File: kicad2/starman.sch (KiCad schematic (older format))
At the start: 60 parts

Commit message: Placements of components and things
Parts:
- added C1, C2, C3, C4, C5, C6: C, Capacitor_SMD:C_0805_2012Metric, symbol Device:C
- added D61, D62, D63, D64, D65, D66, D67, D68, D69, D70, D71, D72, D73, D74, D75, D76, D77, D78, D79, D80, D81, D82, D83, D84, D85, D86, D87, D88, D89: LED, LED_SMD:LED_Osram_Lx_P47F_D2mm_ReverseMount, symbol Device:LED
- added J1: Barrel_Jack, Connector_BarrelJack:BarrelJack_CUI_PJ-036AH-SMT_Horizontal, symbol Connector:Barrel_Jack
- added P1: USB_C_Plug_USB2.0, Connector_USB:USB_C_Plug_JAE_DX07P024AJ1, symbol Connector:USB_C_Plug_USB2.0
- added U1: ESP32-S2-MINI-1, Espressif:ESP32-S2-MINI-1, symbol Espressif:ESP32-S2-MINI-1
- added U2, U3, U4, U5: TLC5947DAP, Package_SO:HTSSOP-32-1EP_6.1x11mm_P0.65mm_EP5.2x11mm_Mask4.11x4.36mm, symbol Driver_LED:TLC5947DAP
- added U6: LF33_TO220, Package_TO_SOT_SMD:SOT-223, symbol Regulator_Linear:LF33_TO220
- added U7: LF50_TO220, Package_TO_SOT_SMD:SOT-223, symbol Regulator_Linear:LF50_TO220
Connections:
- net labels added: +3.3V, +5V, BLANK, BOOT, GND, IREF, RESET, SCLK, SIN, USBDM, USBDP, XLAT
- wire segments 0 -> 296
- no-connect marks 0 -> 12

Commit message: Switch to PCA9959 as LED PWM driver
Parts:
- removed U2, U3, U4, U5: TLC5947DAP, Package_SO:HTSSOP-32-1EP_6.1x11mm_P0.65mm_EP5.2x11mm_Mask4.11x4.36mm, symbol Driver_LED:TLC5947DAP
- added C1: 10uF, Capacitor_SMD:C_0805_2012Metric, symbol Device:C
- added D100, D101, D102, D103, D104, D105, D106, D107, D108, D109, D110, D111, D112, D113, D114, D115, D116, D117, D118, D119, D120, D121, D122, D123, D124, D125, D126, D127, D128, D129, D130, D131, D132, D133, D134, D135, D136, D137, D138, D90, D91, D92, D93, D94, D95, D96, D97, D98, D99: LED, LED_SMD:LED_Osram_Lx_P47F_D2mm_ReverseMount, symbol Device:LED
- added R1, R2, R3: 5.1k, symbol Device:R
- added U2, U3, U4, U5, U8, U9: PCA9959, starman:QFN-40_EP_5x5_Pitch0.4mm, symbol starman:PCA9959
- C2: renamed from C1; value C -> 10uF
- C3: renamed from C2; value C -> 1uF
- P1: footprint Connector_USB:USB_C_Plug_JAE_DX07P024AJ1 -> Connector_USB:USB_C_Plug_Molex_105444; symbol Connector:USB_C_Plug_USB2.0 -> Connector:USB_C_Receptacle_USB2.0
- renumbered C3 to C4, C4 to C5, C5 to C6, C6 to C7
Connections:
- wire segments 296 -> 334
- no-connect marks 12 -> 7
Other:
- moved on the sheet: C2, C3, D1, D10, D11, D12, D13, D14, D15, D16, D17, D18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

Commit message: Route U2 and U3 LEDs
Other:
- moved on the sheet: D1, D10, D11, D12, D13, D14, D15, D16, D17, D18, D19, D2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

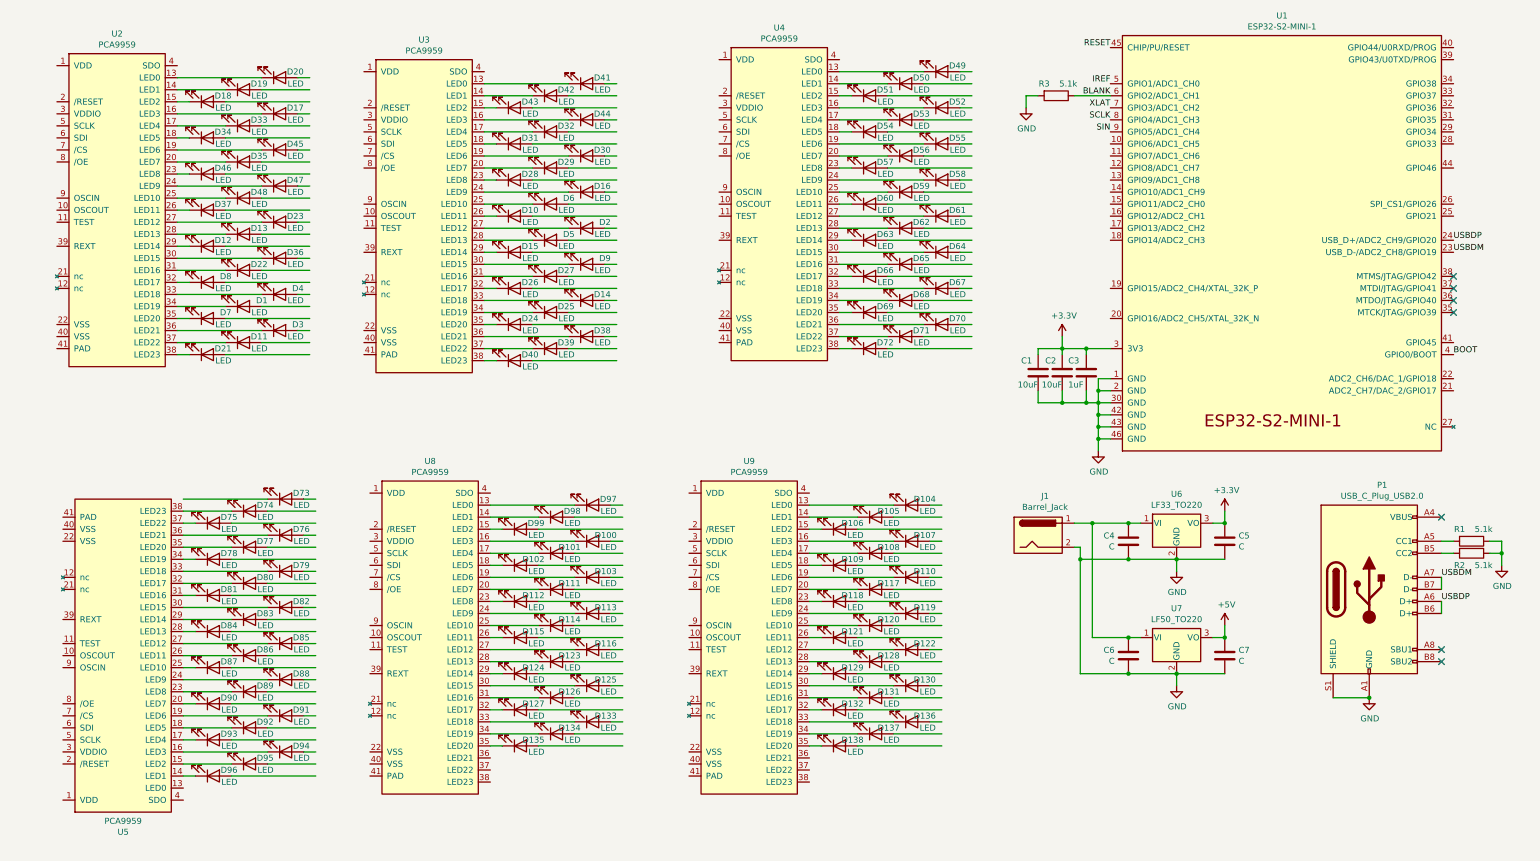
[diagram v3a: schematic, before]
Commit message: Completed tracks to and from LED drivers
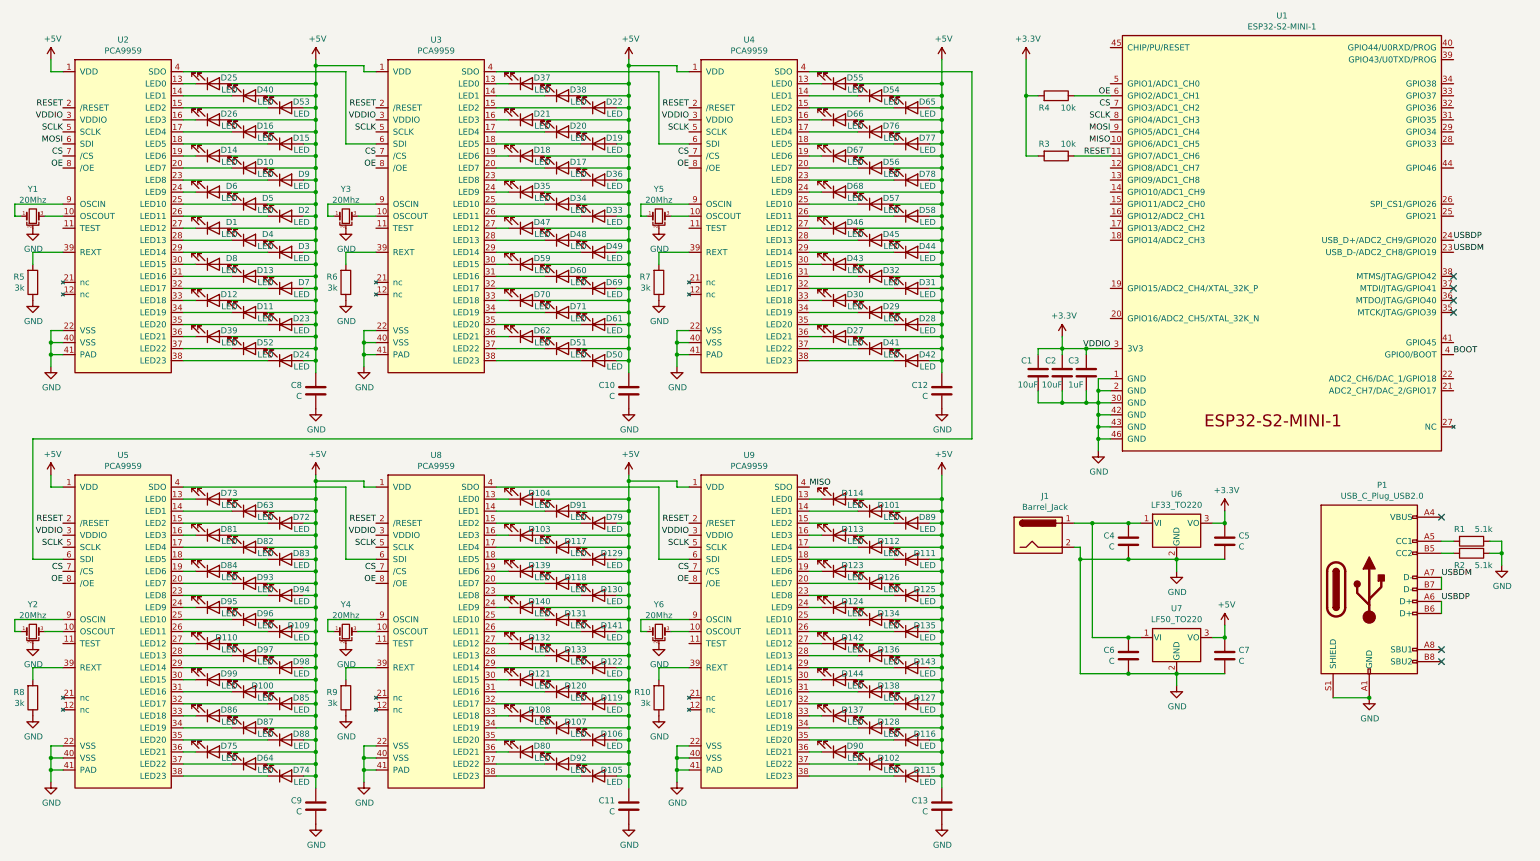
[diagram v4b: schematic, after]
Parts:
- added C10, C11, C12, C13, C8, C9: C, Capacitor_SMD:C_0805_2012Metric, symbol Device:C
- added D139, D140, D141, D142, D143, D144: LED, LED_SMD:LED_Osram_Lx_P47F_D2mm_ReverseMount, symbol Device:LED
- added R10, R5, R6, R7, R8, R9: 3k, Resistor_SMD:R_0805_2012Metric, symbol Device:R
- added R3: 10k, Resistor_SMD:R_0805_2012Metric, symbol Device:R
- added Y1, Y2, Y3, Y4, Y5, Y6: 20Mhz, Crystal:Resonator_SMD_muRata_CSTxExxV-3Pin_3.0x1.1mm, symbol Device:Crystal_GND2_Small
- R1, R2: footprint (none) -> Resistor_SMD:R_0805_2012Metric
- R4: renamed from R3; value 5.1k -> 10k; footprint (none) -> Resistor_SMD:R_0805_2012Metric
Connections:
- net labels added: CS, MISO, MOSI, OE, VDDIO
- net labels removed: BLANK, IREF, SIN, XLAT
- wire segments 334 -> 608
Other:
- moved on the sheet: D1, D10, D100, D101, D102, D103, D104, D105, D106, D107, D108, D109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

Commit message: Added mounting headers -- will move barrel jack and usb to daughter board
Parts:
- removed J1: Barrel_Jack, Connector_BarrelJack:BarrelJack_CUI_PJ-036AH-SMT_Horizontal, symbol Connector:Barrel_Jack
- removed P1: USB_C_Plug_USB2.0, Connector_USB:USB_C_Plug_Molex_105444, symbol Connector:USB_C_Receptacle_USB2.0
- removed R1, R2: 5.1k, Resistor_SMD:R_0805_2012Metric, symbol Device:R
- added J1: Conn_01x10, Connector_PinHeader_2.00mm:PinHeader_1x06_P2.00mm_Vertical_SMD_Pin1Left, symbol Connector_Generic:Conn_01x06
- added J2: Conn_01x10, Connector_PinHeader_2.00mm:PinHeader_1x10_P2.00mm_Vertical_SMD_Pin1Left, symbol Connector_Generic:Conn_01x10
- added J3: Conn_01x10, Connector_PinHeader_2.00mm:PinHeader_1x10_P2.00mm_Vertical_SMD_Pin1Right, symbol Connector_Generic:Conn_01x10
- C6: value C -> 0.1uF
- C7: value C -> 10uF; footprint Capacitor_SMD:C_0805_2012Metric -> Capacitor_Tantalum_SMD:CP_EIA-3216-10_Kemet-I; symbol Device:C -> Device:CP
- U7: value LF50_TO220 -> MIC29310-5.0WU; footprint Package_TO_SOT_SMD:SOT-223 -> Package_TO_SOT_SMD:TO-263-3_TabPin2
- renumbered C12 to C10, C9 to C11, C11 to C12, C10 to C9
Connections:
- net +5V: now also C7.1; no longer C7.2
- net BOOT: now also J1.3 (Pin_3)
- net GND: now also C7.2, J2.3 (Pin_3), J2.4 (Pin_4); no longer C7.1
- net USBDM: now also J1.5 (Pin_5)
- net USBDP: now also J1.6 (Pin_6)
- net TXD: now reaches U1.39 (GPIO43/U0TXD/PROG)
- net TXD: now also J1.1 (Pin_1)
- net RXD: now reaches U1.40 (GPIO44/U0RXD/PROG)
- net RXD: now also J1.2 (Pin_2)
- net ESP_RESET: now reaches U1.45 (CHIP/PU/RESET)
- net ESP_RESET: now also J1.4 (Pin_4)
- net at C4.2, C6.2, U6.1 (VI)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: now also J2.1 (Pin_1), J2.2 (Pin_2)
- no-connect marks 7 -> 4
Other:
- moved on the sheet: C4, C5, C6, U6, U7
